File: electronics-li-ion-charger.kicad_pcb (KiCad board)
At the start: 2 copper layers, 88.9 x 12.7 mm, 20 parts, among them J1 Conn_01x01_Male, J2 Conn_01x01_Male, J3 USB_B_Micro, J4 Conn_01x03_Male, M1 MountingHole_2.2mm_M2, M2 MountingHole_2.2mm_M2, M3 MountingHole_2.2mm_M2, M4 MountingHole_2.2mm_M2, U1 MCP73831-2-OT

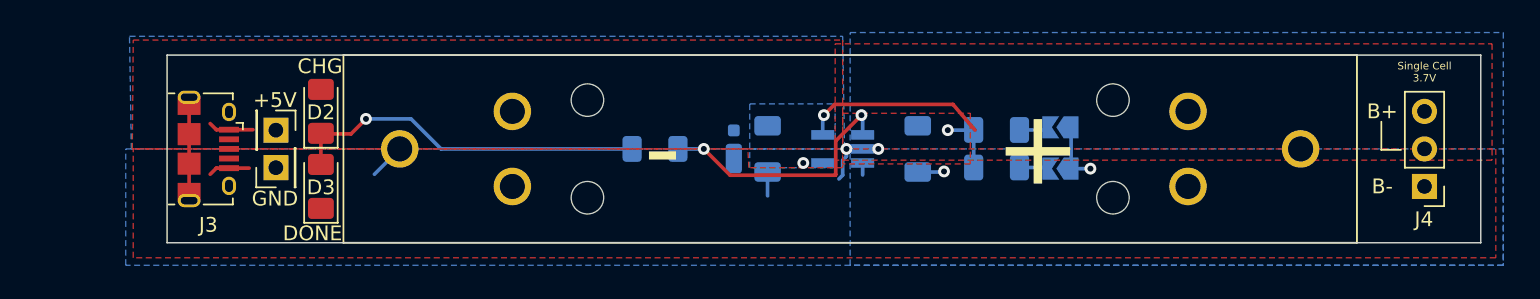
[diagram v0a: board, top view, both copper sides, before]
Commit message: Rev2-1: Fix LED short circuit and PROG trace.
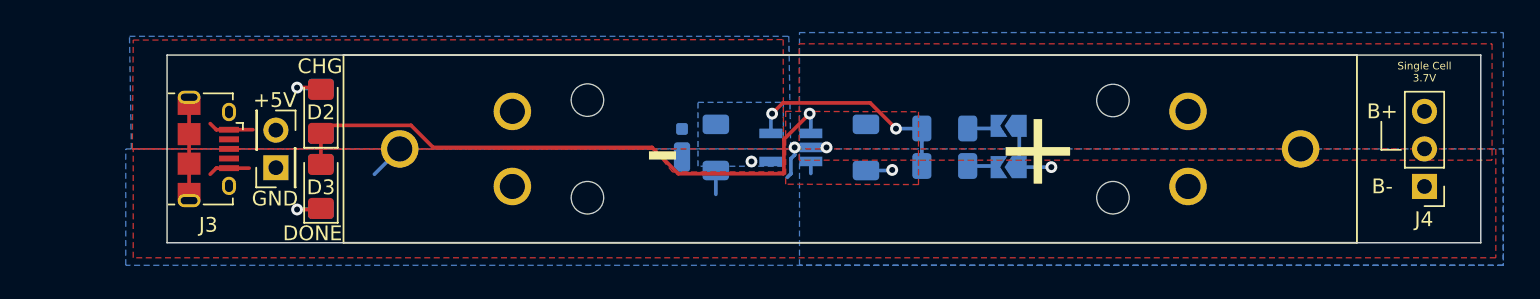
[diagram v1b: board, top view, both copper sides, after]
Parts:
- added R4: 470R, Resistor_SMD:R_1206_3216Metric_Pad1.30x1.75mm_HandSolder, B.Cu at (137.4, 104.1)
- moved R3 22.7 mm to (137.4, 99.0), turned to 270 degrees
- moved M3 6.60 mm to (191.0, 104.9)
- moved M4 6.58 mm to (191.0, 98.3)
- moved JP1 3.51 mm to (183.9, 100.0)
- moved C2 3.51 mm to (174.3, 101.5)
- moved D1 3.51 mm to (161.8, 101.5)
- moved JP2 3.51 mm to (183.9, 102.8)
- moved U1 3.51 mm to (169.2, 101.5)
- moved R1 3.51 mm to (179.6, 100.2)
- moved C1 3.51 mm to (164.1, 101.5)
- moved R2 3.51 mm to (179.6, 102.8)
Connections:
- D2 pad 1: Net-(D2-Pad1) -> STAT
- D2 pad 2: +5V -> Net-(D2-Pad2)
- D3 pad 1: GND -> Net-(D3-Pad1)
- D3 pad 2: Net-(D2-Pad1) -> STAT
- R3 pad 1: STAT -> Net-(D2-Pad2)
- R3 pad 2: Net-(D2-Pad1) -> +5V
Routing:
- net Net-(D2-Pad1): track 24.4 -> 0.00 mm, vias 1 -> 0
- net STAT: track 17.7 -> 41.2 mm, vias 2 -> 1
- net Net-(D3-Pad1): track 0.00 -> 3.39 mm, vias 0 -> 1
- net Net-(D2-Pad2): track 0.00 -> 3.34 mm, vias 0 -> 1
- net PROG: track 17.6 -> 15.7 mm
- net GND: track 17.1 -> 18.0 mm
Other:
- board text added: "13 February 2021"
- board text added: "2-1"
- board text added: "Li-Ion Charger"
- board text added: "Li-Ion Charger Rev2-1 Alexander Fraser 13 February 2021"
- board text removed: "Li-Ion Charger Rev2-0 Alexander Fraser 17 January 2021"

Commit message: Rev3-0: Add reverse polarity protection.
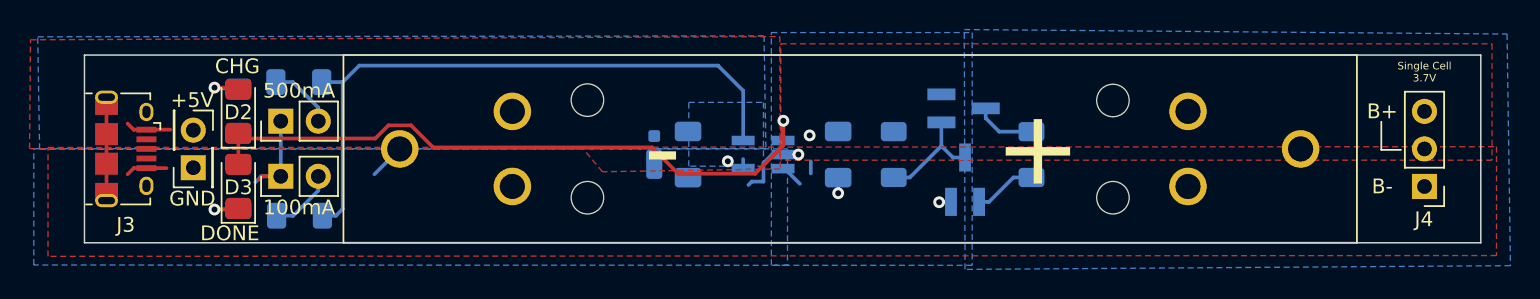
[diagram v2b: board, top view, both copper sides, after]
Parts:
- added Q1: Q_PMOS_DGS, Package_TO_SOT_SMD:SOT-23_Handsoldering, B.Cu at (180.9, 98.9)
- added Q2: Q_NPN_BCE, Package_TO_SOT_SMD:SOT-23_Handsoldering, B.Cu at (181.0, 103.7)
- added R5: 10K, Resistor_SMD:R_1206_3216Metric_Pad1.30x1.75mm_HandSolder, B.Cu at (176.2, 102.0)
- added R6: 10K, Resistor_SMD:R_1206_3216Metric_Pad1.30x1.75mm_HandSolder, B.Cu at (185.5, 102.0)
- JP1, JP2: footprint Jumper:SolderJumper-2_P1.3mm_Open_TrianglePad1.0x1.5mm -> Connector_PinHeader_2.54mm:PinHeader_1x02_P2.54mm_Vertical; moved to F.Cu
- moved JP2 49.3 mm to (134.7, 103.5), turned to 90 degrees
- moved JP1 49.3 mm to (134.7, 99.7), turned to 90 degrees
- moved R1 43.8 mm to (135.9, 97.1), turned to 180 degrees
- moved R2 43.8 mm to (136.0, 106.1), turned to 180 degrees
- moved J1 5.59 mm to (128.8, 100.3)
- moved J2 5.59 mm to (128.8, 102.9)
- moved J3 5.59 mm to (124.2, 101.6)
- moved D2 5.59 mm to (131.8, 99.1)
- moved D3 5.59 mm to (131.8, 104.1)
- moved R3 5.59 mm to (131.8, 99.0)
- moved R4 5.59 mm to (131.8, 104.1)
- moved C1 1.94 mm to (162.3, 102.0)
- moved C2 1.94 mm to (172.4, 102.0)
- moved D1 1.94 mm to (160.0, 102.0)
- moved U1 1.94 mm to (167.3, 102.0)
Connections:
- BT1 pad 1: /VBAT -> PROT
- C2 pad 1: /VBAT -> VBAT
- J4 pad 2: /VBAT -> PROT
- J4 pad 3: /VBAT -> PROT
- U1 pad 3: /VBAT -> VBAT
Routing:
- net PROG: track 15.7 -> 43.2 mm, vias 2 -> 0
- net Net-(Q1-Pad1): track 0.00 -> 7.68 mm
- net STAT: track 41.2 -> 46.0 mm
- net Net-(Q2-Pad1): track 0.00 -> 4.23 mm
- net PROT: track 0.00 -> 4.14 mm
- net Net-(JP2-Pad2): track 2.07 -> 4.49 mm
- net Net-(JP1-Pad2): track 2.12 -> 4.50 mm
- net VBAT: track 0.00 -> 2.38 mm, vias 0 -> 1
- net /VBAT: track 0.81 -> 0.00 mm
- net +5V: track 3.06 -> 3.70 mm
- net GND: track 18.0 -> 18.2 mm, vias 4 -> 3
- added copper zone on B.Cu, net PROT
- added copper zone on B.Cu, net VBAT
- added copper zone on F.Cu, net VBAT
- removed copper zone on B.Cu, net /VBAT
- removed copper zone on F.Cu, net /VBAT
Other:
- board size 88.9 x 12.7 mm -> 94.5 x 12.7 mm
- board text added: "19 February 2021"
- board text added: "3-0"
- board text added: "3-0: Add reverse polarity protection. Change current selection to header pins."
- board text added: "Li-Ion Charger Rev3-0 Alexander Fraser 19 February 2021"
- board text removed: "13 February 2021"
- board text removed: "2-1"
- board text removed: "Li-Ion Charger Rev2-1 Alexander Fraser 13 February 2021"
